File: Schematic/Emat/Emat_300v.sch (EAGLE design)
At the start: 64 parts, among them IC1 UC3843N, J1 PIN1-2, J2 PIN1-2, J3 PIN1-2, J4 PIN1-2, J5 PIN1-2, J6 PIN1-2, Q1 BSS138, Q2 IRF640IW220B, T1 EFD25-2

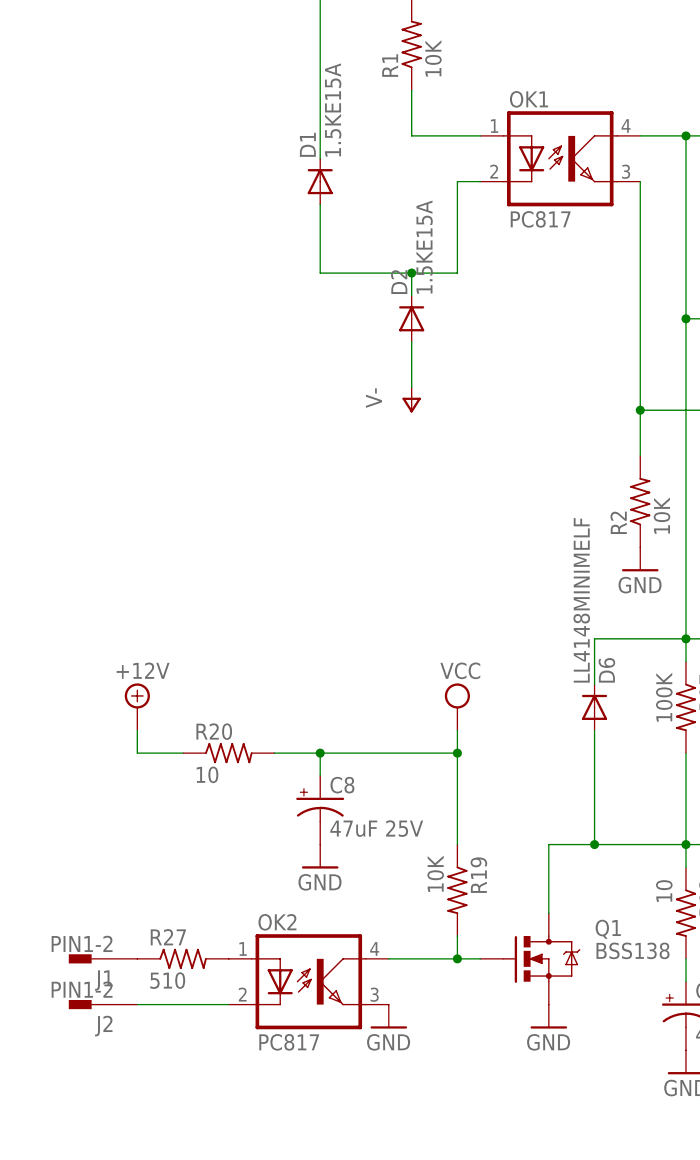
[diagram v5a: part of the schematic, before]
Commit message: Fix schematic. 1.5KE300 added.
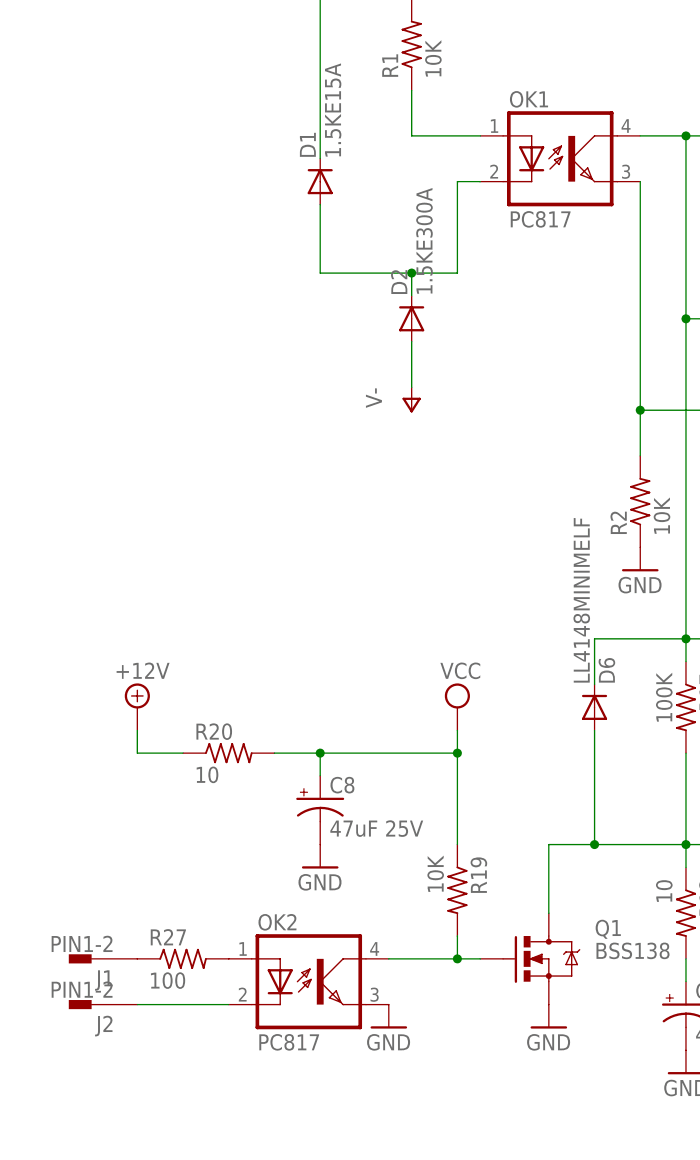
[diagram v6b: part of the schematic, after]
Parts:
- D2: value 1.5KE15A -> 1.5KE300A
- R27: value 510 -> 100
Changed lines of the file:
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@@
 <parts>
 <part name="D1" library="diode" deviceset="DIODE-" device="DO201-15" value="1.5KE15A"/>
-<part name="D2" library="diode" deviceset="DIODE-" device="DO201-15" value="1.5KE15A"/>
+<part name="D2" library="diode" deviceset="DIODE-" device="DO201-15" value="1.5KE300A"/>
 <part name="R1" library="resistor" deviceset="R-US_" device="R1206" value="10K"/>
 <part name="OK1" library="optocoupler" deviceset="PC817" device=""/>
@@
 <part name="P-3" library="supply1" deviceset="V-" device=""/>
 <part name="P+3" library="supply1" deviceset="V+" device=""/>
-<part name="R27" library="resistor" deviceset="R-US_" device="R1206" value="510"/>
+<part name="R27" library="resistor" deviceset="R-US_" device="R1206" value="100"/>
 </parts>
 <sheets>
